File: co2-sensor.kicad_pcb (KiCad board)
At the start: 2 copper layers, 61 x 61 mm, 51 parts, among them J1 24-pin FPC Connector, J2 USB-C Receptacle, J3 JST 2-PH, Q1 AO3401A, Q2 AO3400A, SW1 SW_Push, SW2 SW_Push, SW3 SW_Push, SW4 SW_Push, SW5 SW_Push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

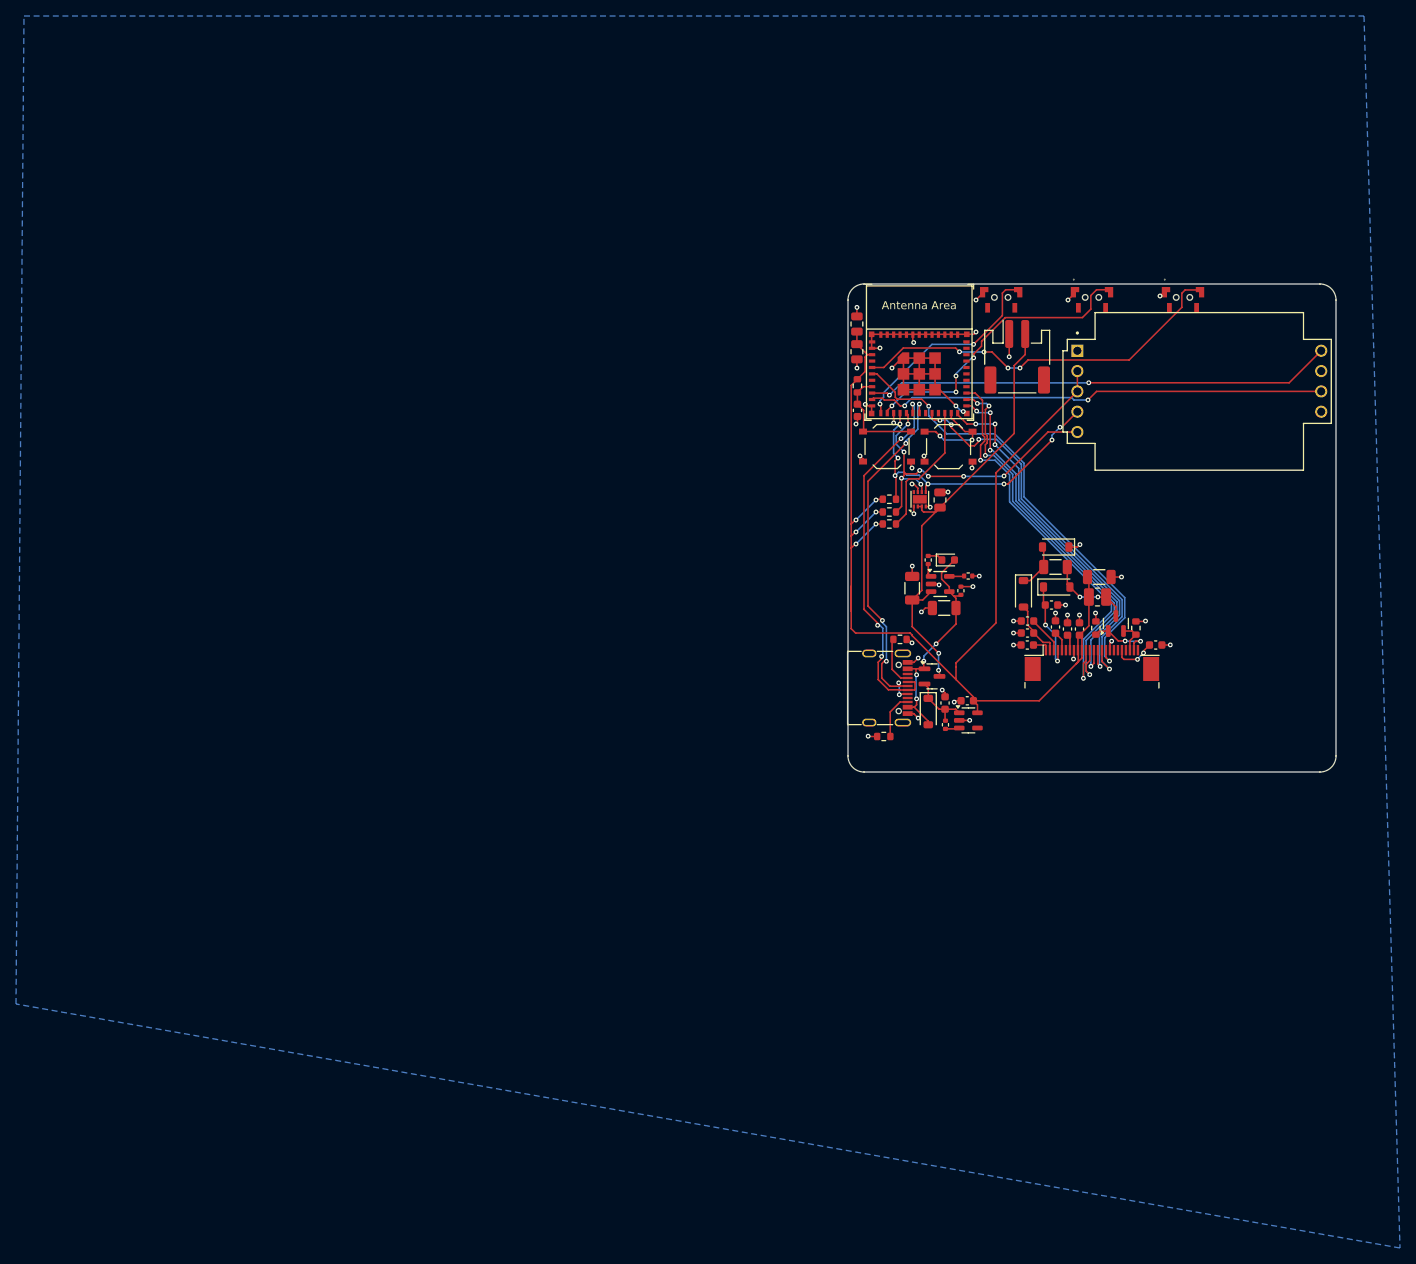
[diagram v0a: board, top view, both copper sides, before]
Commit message: Add labels and OSHW logo
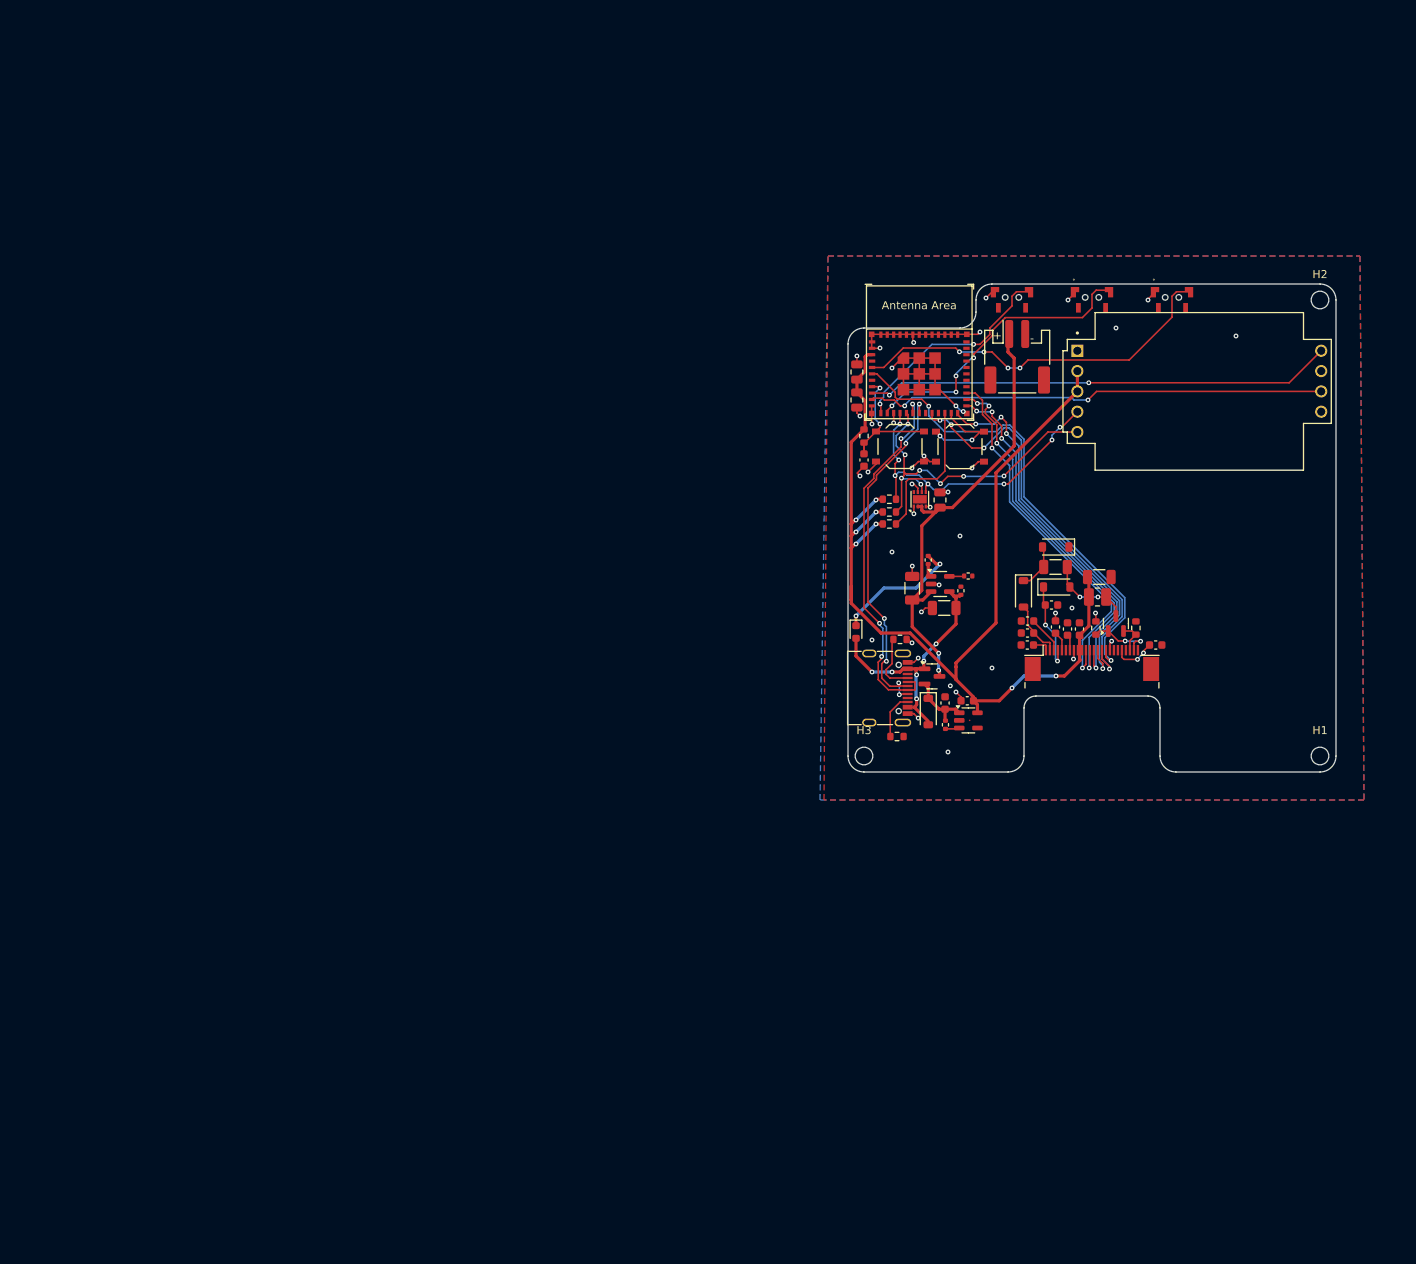
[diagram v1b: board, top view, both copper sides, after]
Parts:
- added H1: MountingHole, MountingHole:MountingHole_2.2mm_M2, F.Cu at (190.0, 131.0)
- added H2: MountingHole, MountingHole:MountingHole_2.2mm_M2, F.Cu at (190.0, 74.0)
- added H3: MountingHole, MountingHole:MountingHole_2.2mm_M2, F.Cu at (133.0, 131.0)
- added REF**: OSHW-Logo2_14.6x12mm_SilkScreen, Symbol:OSHW-Logo2_14.6x12mm_SilkScreen, B.Cu at (179.5, 124.5)
- moved D5 14.6 mm to (132.0, 115.5), turned to -90 degrees
- moved R7 6.32 mm to (133.0, 91.0)
- moved C13 6.26 mm to (133.0, 94.0)
- moved C17 6.03 mm to (132.1, 86.5)
- moved C16 6.00 mm to (132.1, 83.0)
- moved R4 1.65 mm to (137.1, 128.6), turned to 180 degrees
- moved SW1 1.62 mm to (137.5, 92.3)
- moved SW2 1.43 mm to (145.0, 92.3)
- moved SW5 1.38 mm to (171.5, 74.0)
- moved SW3 1.35 mm to (151.5, 74.0)
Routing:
- net Net-(D5-K): track 1.92 -> 16.3 mm, vias 0 -> 2
- net GND: track 97.8 -> 84.6 mm, vias 49 -> 42
- net +3.3V: track 154.1 -> 145.0 mm, vias 6 -> 8
- net VBUS: track 28.5 -> 33.2 mm, vias 4 -> 6
- net /EN: track 13.4 -> 18.0 mm, vias 0 -> 2
- net /EINK_MOSI: track 50.4 -> 46.4 mm
- net /EINK_SCLK: track 49.5 -> 46.3 mm
- net /EINK_RES: track 50.2 -> 53.2 mm
- net /EINK_BUSY: track 57.5 -> 60.1 mm
- net /EINK_DC: track 45.3 -> 47.8 mm
- net Net-(J2-CC1): track 6.15 -> 7.56 mm
- net /BOOT8: track 17.1 -> 18.5 mm
- net /BTN1: track 26.7 -> 27.8 mm
- net /BTN3: track 48.2 -> 47.2 mm
- net /BOOT9: track 11.4 -> 12.3 mm
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- added copper zone on F.Cu, net GND
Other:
- outline, holes or cut-outs redrawn
- board text added: "+"
- board text added: "-"
- board text added: "CO2 Sensor"
- board text added: "blinry.org"
- board text added: "v0.1"

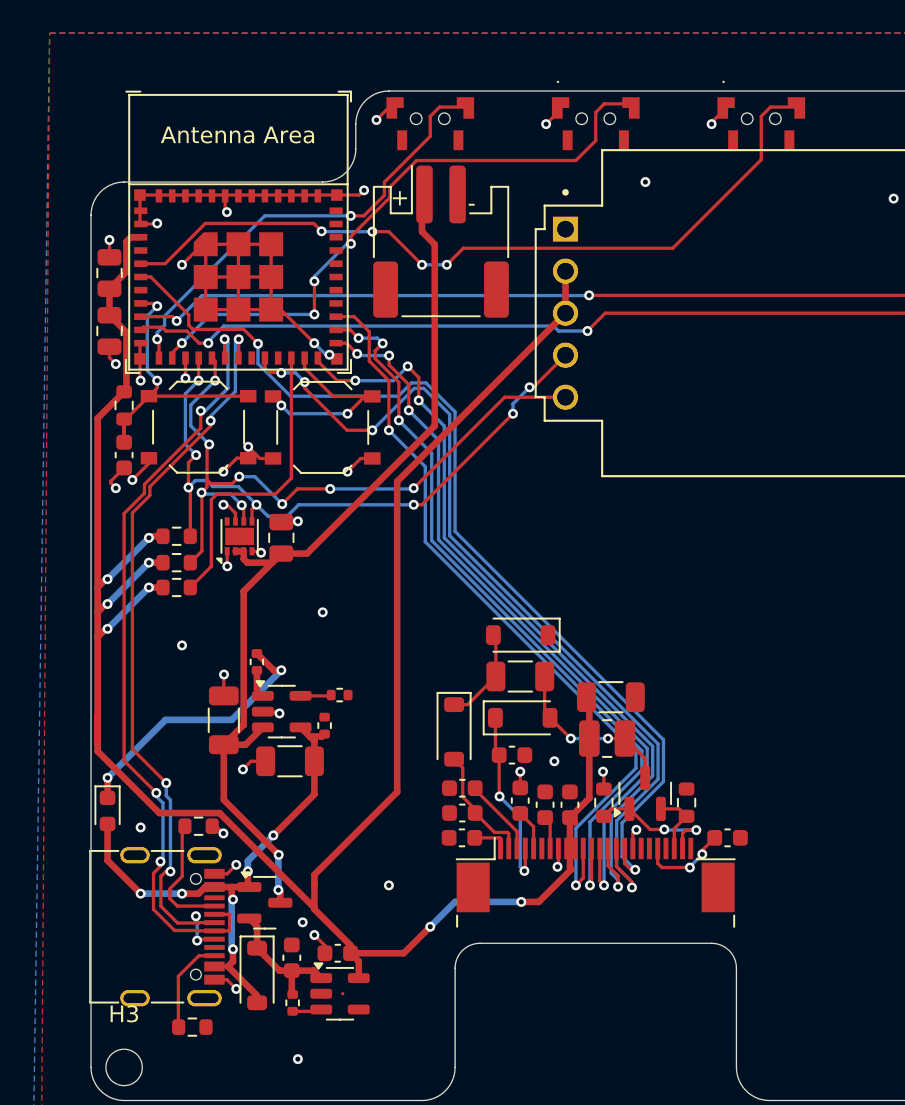
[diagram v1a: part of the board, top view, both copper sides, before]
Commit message: Fix more distance violations
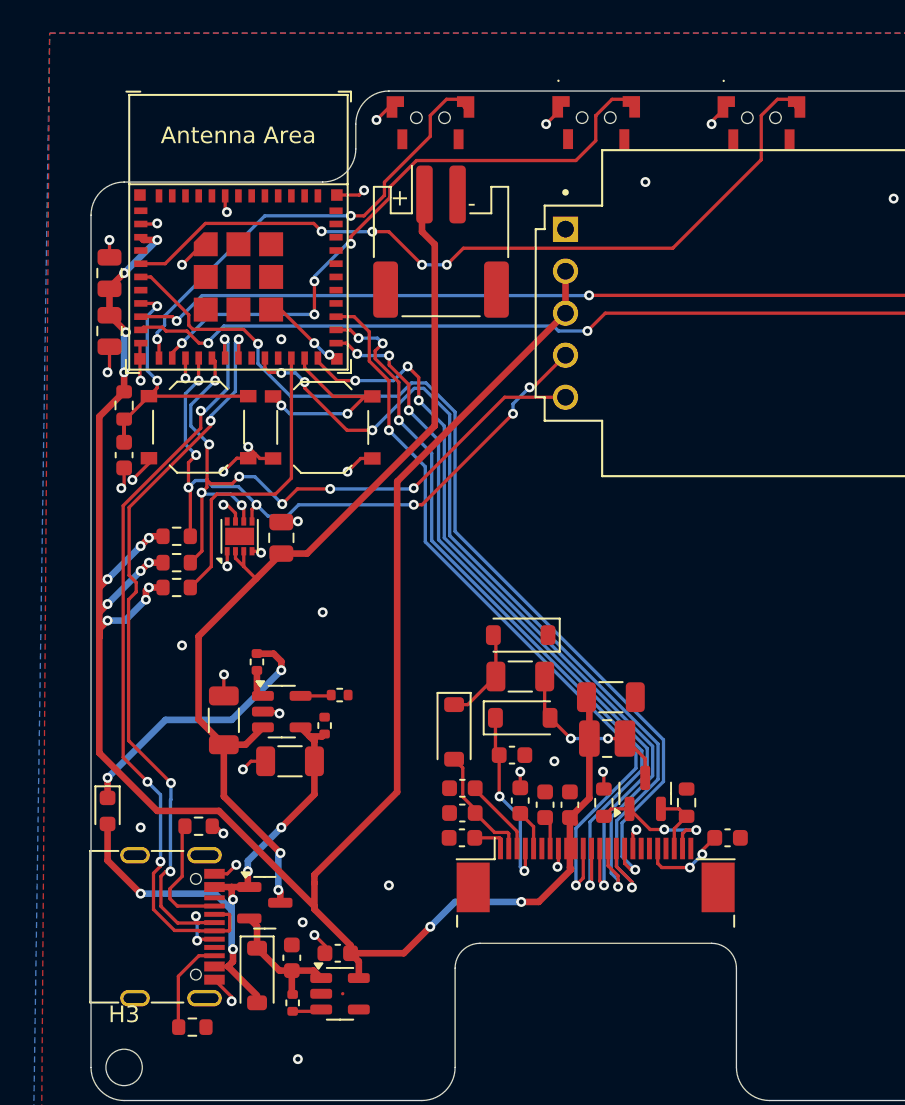
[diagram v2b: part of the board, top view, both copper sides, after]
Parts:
- moved SW4 0.07 mm to (161.5, 73.9)
- moved SW3 0.06 mm to (151.5, 73.9)
- moved SW5 0.06 mm to (171.5, 73.9)
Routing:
- net GND: track 84.6 -> 47.6 mm, vias 42 -> 43
- net VBUS: track 33.2 -> 34.5 mm, vias 6 -> 5
- net +BATT: track 57.2 -> 58.0 mm
- net /D+: track 46.2 -> 46.7 mm
- net +3.3V: track 145.0 -> 144.7 mm, vias 8 -> 15

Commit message: Lower general clerance to 0.1 mm
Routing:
- net +3.3V: vias 15 -> 12
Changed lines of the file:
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@@
-	)
-	(via
-		(at 134.5 102)
-		(size 0.6)
-		(drill 0.3)
-		(layers "F.Cu" "B.Cu")
-		(net 7)
 	)
 	(via
 		(at 134 99.5)
-		(size 0.6)
-		(drill 0.3)
-		(layers "F.Cu" "B.Cu")
-		(net 7)
-	)
-	(via
-		(at 134.5 100.5)
 		(size 0.6)
 		(drill 0.3)
@@
 		(size 0.6)
 		(drill 0.3)
-		(layers "F.Cu" "B.Cu")
-		(net 7)
-	)
-	(via
-		(at 134.5 99)
-		(size 0.6)
-		(drill 0.3)

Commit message: Add pins for providing BAT power
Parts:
- removed REF**: OSHW-Logo2_14.6x12mm_SilkScreen, Symbol:OSHW-Logo2_14.6x12mm_SilkScreen
- added J4: Conn_02x01, Connector_PinHeader_2.54mm:PinHeader_1x02_P2.54mm_Vertical, F.Cu at (180.0, 73.5)
- added JP1: SolderJumper_2_Bridged, Jumper:SolderJumper-2_P1.3mm_Bridged_RoundedPad1.0x1.5mm, F.Cu at (147.8, 113.0)
- moved R14 2.68 mm to (143.0, 112.0), turned to 0 degrees
- moved C14 1.50 mm to (143.0, 114.0)
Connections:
- U3 pad 4: VBUS -> Net-(JP1-B)
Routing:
- net +BATT: track 58.0 -> 91.7 mm, vias 2 -> 4
- net Net-(JP1-B): track 0.00 -> 6.77 mm
- net GND: track 47.6 -> 51.7 mm, vias 43 -> 46
- net VBUS: track 34.5 -> 35.2 mm
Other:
- board text added: "BAT"
- board text added: "Disable LiPo charger"
- board text added: "GND"
- board text added: "Senseair Sunrise/Sunlight"

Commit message: Improve labels
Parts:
- added REF**: OSHW-Logo_11.4x12mm_Copper, Symbol:OSHW-Logo_11.4x12mm_Copper, B.Cu at (182.8, 123.1)
- moved A1 1.00 mm to (173.9, 85.5)
- moved H1 0.71 mm to (189.5, 130.5)
- moved H2 0.71 mm to (189.5, 74.5)
- moved H3 0.71 mm to (133.5, 130.5)
- moved J3 0.14 mm to (152.0, 81.1)
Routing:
- net /CO2_NRDY: track 57.7 -> 56.6 mm
- net /I2C_SCL: track 43.1 -> 42.1 mm
- net /CO2_EN: track 58.6 -> 57.6 mm
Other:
- board text added: "CO2 Canary"
- board text added: "v0.1.0"
- board text removed: "CO2 Sensor"
- board text removed: "v0.1"
